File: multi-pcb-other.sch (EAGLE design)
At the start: 6 parts

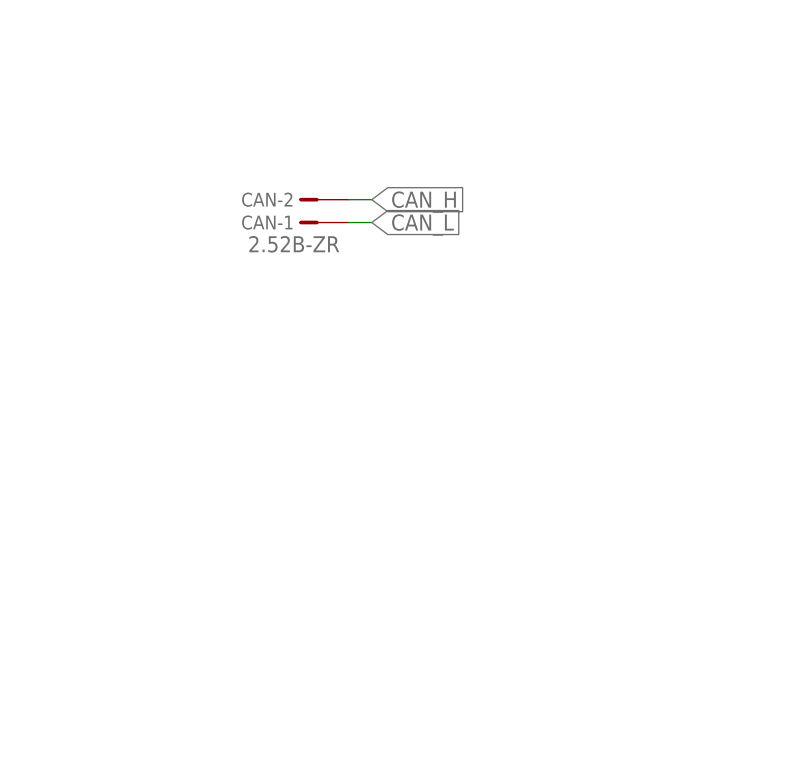
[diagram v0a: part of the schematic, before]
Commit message: Routed more multi-pcb boards
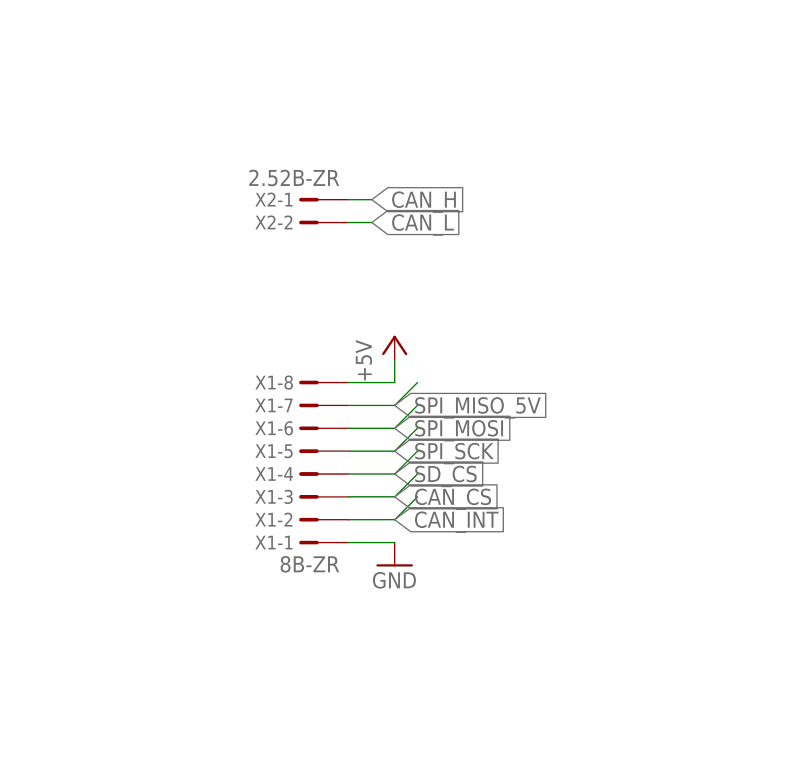
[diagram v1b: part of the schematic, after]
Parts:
- removed CAN: 2.52B-ZR, con-jst-custom:2.52B-ZR
- added X1: 8B-ZR, con-jst-custom:8B-ZR
- added X2: 2.52B-ZR, con-jst-custom:2.52B-ZR
- R14: device rcl:R-EU_0309/10 -> rcl:R-EU_0207/7
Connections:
- net +5V: now also X1-8.1
- net CAN_CS: now also X1-3.1
- net CAN_H: now also X2-1.1; no longer CAN-2.1
- net CAN_INT: now also X1-2.1
- net CAN_L: now also X2-2.1; no longer CAN-1.1
- net GND: now also X1-1.1
- net SD_CS: now also X1-4.1
- net SPI_MISO_5V: now also X1-7.1
- net SPI_MOSI: now also X1-6.1
- net SPI_SCK: now also X1-5.1
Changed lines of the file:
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@@
 <part name="GND7" library="supply1" library_urn="urn:adsk.eagle:library:371" deviceset="GND" device=""/>
 <part name="P+1" library="supply1" library_urn="urn:adsk.eagle:library:371" deviceset="+5V" device=""/>
-<part name="CAN" library="con-jst-custom" deviceset="?2B-ZR" device="2.5" value="2.52B-ZR"/>
 <part name="U$5" library="sd-mmc" deviceset="HKD-MICRO-SD-BREAKOUT" device="H"/>
 <part name="GND24" library="supply1" library_urn="urn:adsk.eagle:library:371" deviceset="GND" device=""/>
 <part name="P+19" library="supply1" library_urn="urn:adsk.eagle:library:371" deviceset="+5V" device=""/>
-<part name="R14" library="rcl" library_urn="urn:adsk.eagle:library:334" deviceset="R-EU_" device="0309/10" package3d_urn="urn:adsk.eagle:package:23567/2" value="2k"/>
+<part name="R14" library="rcl" library_urn="urn:adsk.eagle:library:334" deviceset="R-EU_" device="0207/7" package3d_urn="urn:adsk.eagle:package:23493/2" value="2k"/>
 <part name="R15" library="rcl" library_urn="urn:adsk.eagle:library:334" deviceset="R-EU_" device="0207/7" package3d_urn="urn:adsk.eagle:package:23493/2" value="5k"/>
 <part name="GND30" library="supply1" library_urn="urn:adsk.eagle:library:371" deviceset="GND" device=""/>
 <part name="CAN_TERM_RESISTOR" library="pinhead" library_urn="urn:adsk.eagle:library:325" deviceset="PINHD-1X2" device="" package3d_urn="urn:adsk.eagle:package:22435/2"/>
+<part name="GND1" library="supply1" library_urn="urn:adsk.eagle:library:371" deviceset="GND" device=""/>
+<part name="P+2" library="supply1" library_urn="urn:adsk.eagle:library:371" deviceset="+5V" device=""/>
+<part name="X1" library="con-jst-custom" deviceset="?8B-ZR" device=""/>
+<part name="X2" library="con-jst-custom" deviceset="?2B-ZR" device="2.5"/>
 </parts>
 <sheets>
@@
 <attribute name="VALUE" x="-63.5" y="124.46" size="1.778" layer="96" rot="R180"/>
 </instance>
-<instance part="CAN" gate="-1" x="-167.64" y="96.52" smashed="yes" rot="R180">
-<attribute name="NAME" x="-168.656" y="97.282" size="1.524" layer="95" rot="R180"/>
-<attribute name="VALUE" x="-163.576" y="94.996" size="1.778" layer="96" rot="R180"/>
-</instance>
-<instance part="CAN" gate="-2" x="-167.64" y="99.06" smashed="yes" rot="R180">
-<attribute name="NAME" x="-168.656" y="99.822" size="1.524" layer="95" rot="R180"/>
-</instance>
 <instance part="U$5" gate="G$1" x="50.8" y="78.74" smashed="yes"/>
 <instance part="GND24" gate="1" x="33.02" y="68.58" smashed="yes">
@@
 <attribute name="NAME" x="-176.53" y="-10.795" size="1.778" layer="95" rot="R180"/>
 <attribute name="VALUE" x="-176.53" y="0" size="1.778" layer="96" rot="R180"/>
+</instance>
+<instance part="GND1" gate="1" x="-157.48" y="58.42" smashed="yes">
+<attribute name="VALUE" x="-160.02" y="55.88" size="1.778" layer="96"/>
+</instance>
+<instance part="P+2" gate="1" x="-157.48" y="83.82" smashed="yes">
+<attribute name="VALUE" x="-160.02" y="78.74" size="1.778" layer="96" rot="R90"/>
+</instance>
+<instance part="X1" gate="-1" x="-167.64" y="60.96" smashed="yes" rot="R180">
+<attribute name="NAME" x="-168.656" y="61.722" size="1.524" layer="95" rot="R180"/>
+<attribute name="VALUE" x="-163.576" y="59.436" size="1.778" layer="96" rot="R180"/>
+</instance>
+<instance part="X1" gate="-2" x="-167.64" y="63.5" smashed="yes" rot="R180">
+<attribute name="NAME" x="-168.656" y="64.262" size="1.524" layer="95" rot="R180"/>
+</instance>
+<instance part="X1" gate="-3" x="-167.64" y="66.04" smashed="yes" rot="R180">
+<attribute name="NAME" x="-168.656" y="66.802" size="1.524" layer="95" rot="R180"/>
+</instance>
+<instance part="X1" gate="-4" x="-167.64" y="68.58" smashed="yes" rot="R180">
+<attribute name="NAME" x="-168.656" y="69.342" size="1.524" layer="95" rot="R180"/>
+</instance>
+<instance part="X1" gate="-5" x="-167.64" y="71.12" smashed="yes" rot="R180">
+<attribute name="NAME" x="-168.656" y="71.882" size="1.524" layer="95" rot="R180"/>
+</instance>
+<instance part="X1" gate="-6" x="-167.64" y="73.66" smashed="yes" rot="R180">
+<attribute name="NAME" x="-168.656" y="74.422" size="1.524" layer="95" rot="R180"/>
+</instance>
+<instance part="X1" gate="-7" x="-167.64" y="76.2" smashed="yes" rot="R180">
+<attribute name="NAME" x="-168.656" y="76.962" size="1.524" layer="95" rot="R180"/>
+</instance>
+<instance part="X1" gate="-8" x="-167.64" y="78.74" smashed="yes" rot="R180">
+<attribute name="NAME" x="-168.656" y="79.502" size="1.524" layer="95" rot="R180"/>
+</instance>
+<instance part="X2" gate="-1" x="-167.64" y="99.06" smashed="yes" rot="MR0">
+<attribute name="NAME" x="-168.656" y="98.298" size="1.524" layer="95" rot="MR0"/>
+<attribute name="VALUE" x="-163.576" y="100.584" size="1.778" layer="96" rot="MR0"/>
+</instance>
+<instance part="X2" gate="-2" x="-167.64" y="96.52" smashed="yes" rot="MR0">
+<attribute name="NAME" x="-168.656" y="95.758" size="1.524" layer="95" rot="MR0"/>
 </instance>
 </instances>
@@
 <wire x1="-53.34" y1="157.48" x2="-50.8" y2="157.48" width="0.1524" layer="91"/>
 </segment>
+<segment>
+<pinref part="X1" gate="-1" pin="1"/>
+<pinref part="GND1" gate="1" pin="GND"/>
+<wire x1="-162.56" y1="60.96" x2="-157.48" y2="60.96" width="0.1524" layer="91"/>
+</segment>
 </net>
 <net name="+5V" class="0">
@@
 <wire x1="35.56" y1="73.66" x2="27.94" y2="73.66" width="0.1524" layer="91"/>
 <pinref part="P+19" gate="1" pin="+5V"/>
+</segment>
+<segment>
+<pinref part="P+2" gate="1" pin="+5V"/>
+<wire x1="-157.48" y1="81.28" x2="-157.48" y2="78.74" width="0.1524" layer="91"/>
+<pinref part="X1" gate="-8" pin="1"/>
+<wire x1="-162.56" y1="78.74" x2="-157.48" y2="78.74" width="0.1524" layer="91"/>
 </segment>
 </net>
@@
 <label x="-86.36" y="144.78" size="1.778" layer="95" rot="R90" xref="yes"/>
 </segment>
+<segment>
+<label x="-157.48" y="66.04" size="1.778" layer="95" xref="yes"/>
+<wire x1="-157.48" y1="66.04" x2="-154.94" y2="68.58" width="0.1524" layer="91"/>
+<pinref part="X1" gate="-3" pin="1"/>
+<wire x1="-162.56" y1="66.04" x2="-157.48" y2="66.04" width="0.1524" layer="91"/>
+</segment>
 </net>
 <net name="SPI_MOSI" class="0">
@@
 <label x="33.02" y="78.74" size="1.778" layer="95" rot="R180" xref="yes"/>
 </segment>
+<segment>
+<label x="-157.48" y="73.66" size="1.778" layer="95" xref="yes"/>
+<wire x1="-157.48" y1="73.66" x2="-154.94" y2="76.2" width="0.1524" layer="91"/>
+<pinref part="X1" gate="-6" pin="1"/>
+<wire x1="-162.56" y1="73.66" x2="-157.48" y2="73.66" width="0.1524" layer="91"/>
+</segment>
 </net>
 <net name="SPI_SCK" class="0">
@@
 <wire x1="35.56" y1="81.28" x2="33.02" y2="81.28" width="0.1524" layer="91"/>
 <label x="33.02" y="81.28" size="1.778" layer="95" rot="R180" xref="yes"/>
+</segment>
+<segment>
+<label x="-157.48" y="71.12" size="1.778" layer="95" xref="yes"/>
+<wire x1="-157.48" y1="71.12" x2="-154.94" y2="73.66" width="0.1524" layer="91"/>
+<pinref part="X1" gate="-5" pin="1"/>
+<wire x1="-162.56" y1="71.12" x2="-157.48" y2="71.12" width="0.1524" layer="91"/>
 </segment>
 </net>
@@
 <label x="-66.04" y="160.02" size="1.778" layer="95" rot="R90" xref="yes"/>
 </segment>
+<segment>
+<label x="-157.48" y="63.5" size="1.778" layer="95" xref="yes"/>
+<wire x1="-157.48" y1="63.5" x2="-154.94" y2="66.04" width="0.1524" layer="91"/>
+<pinref part="X1" gate="-2" pin="1"/>
+<wire x1="-162.56" y1="63.5" x2="-157.48" y2="63.5" width="0.1524" layer="91"/>
+</segment>
 </net>
 <net name="CAN_H" class="0">
@@
 </segment>
 <segment>
-<pinref part="CAN" gate="-2" pin="1"/>
 <wire x1="-162.56" y1="99.06" x2="-160.02" y2="99.06" width="0.1524" layer="91"/>
 <label x="-160.02" y="99.06" size="1.778" layer="95" xref="yes"/>
+<pinref part="X2" gate="-1" pin="1"/>
 </segment>
 </net>
@@
 </segment>
 <segment>
-<pinref part="CAN" gate="-1" pin="1"/>
 <wire x1="-162.56" y1="96.52" x2="-160.02" y2="96.52" width="0.1524" layer="91"/>
 <label x="-160.02" y="96.52" size="1.778" layer="95" xref="yes"/>
+<pinref part="X2" gate="-2" pin="1"/>
 </segment>
 </net>
@@
 <wire x1="35.56" y1="83.82" x2="33.02" y2="83.82" width="0.1524" layer="91"/>
 <label x="33.02" y="83.82" size="1.778" layer="95" rot="R180" xref="yes"/>
+</segment>
+<segment>
+<label x="-157.48" y="68.58" size="1.778" layer="95" xref="yes"/>
+<wire x1="-157.48" y1="68.58" x2="-154.94" y2="71.12" width="0.1524" layer="91"/>
+<pinref part="X1" gate="-4" pin="1"/>
+<wire x1="-162.56" y1="68.58" x2="-157.48" y2="68.58" width="0.1524" layer="91"/>
 </segment>
 </net>
@@
 <label x="33.02" y="76.2" size="1.778" layer="95" rot="R180" xref="yes"/>
 </segment>
-</net>
+<segment>
+<label x="-157.48" y="76.2" size="1.778" layer="95" xref="yes"/>
+<wire x1="-157.48" y1="76.2" x2="-154.94" y2="78.74" width="0.1524" layer="91"/>
+<pinref part="X1" gate="-7" pin="1"/>
+<wire x1="-162.56" y1="76.2" x2="-157.48" y2="76.2" width="0.1524" layer="91"/>
+</segment>
+</net>

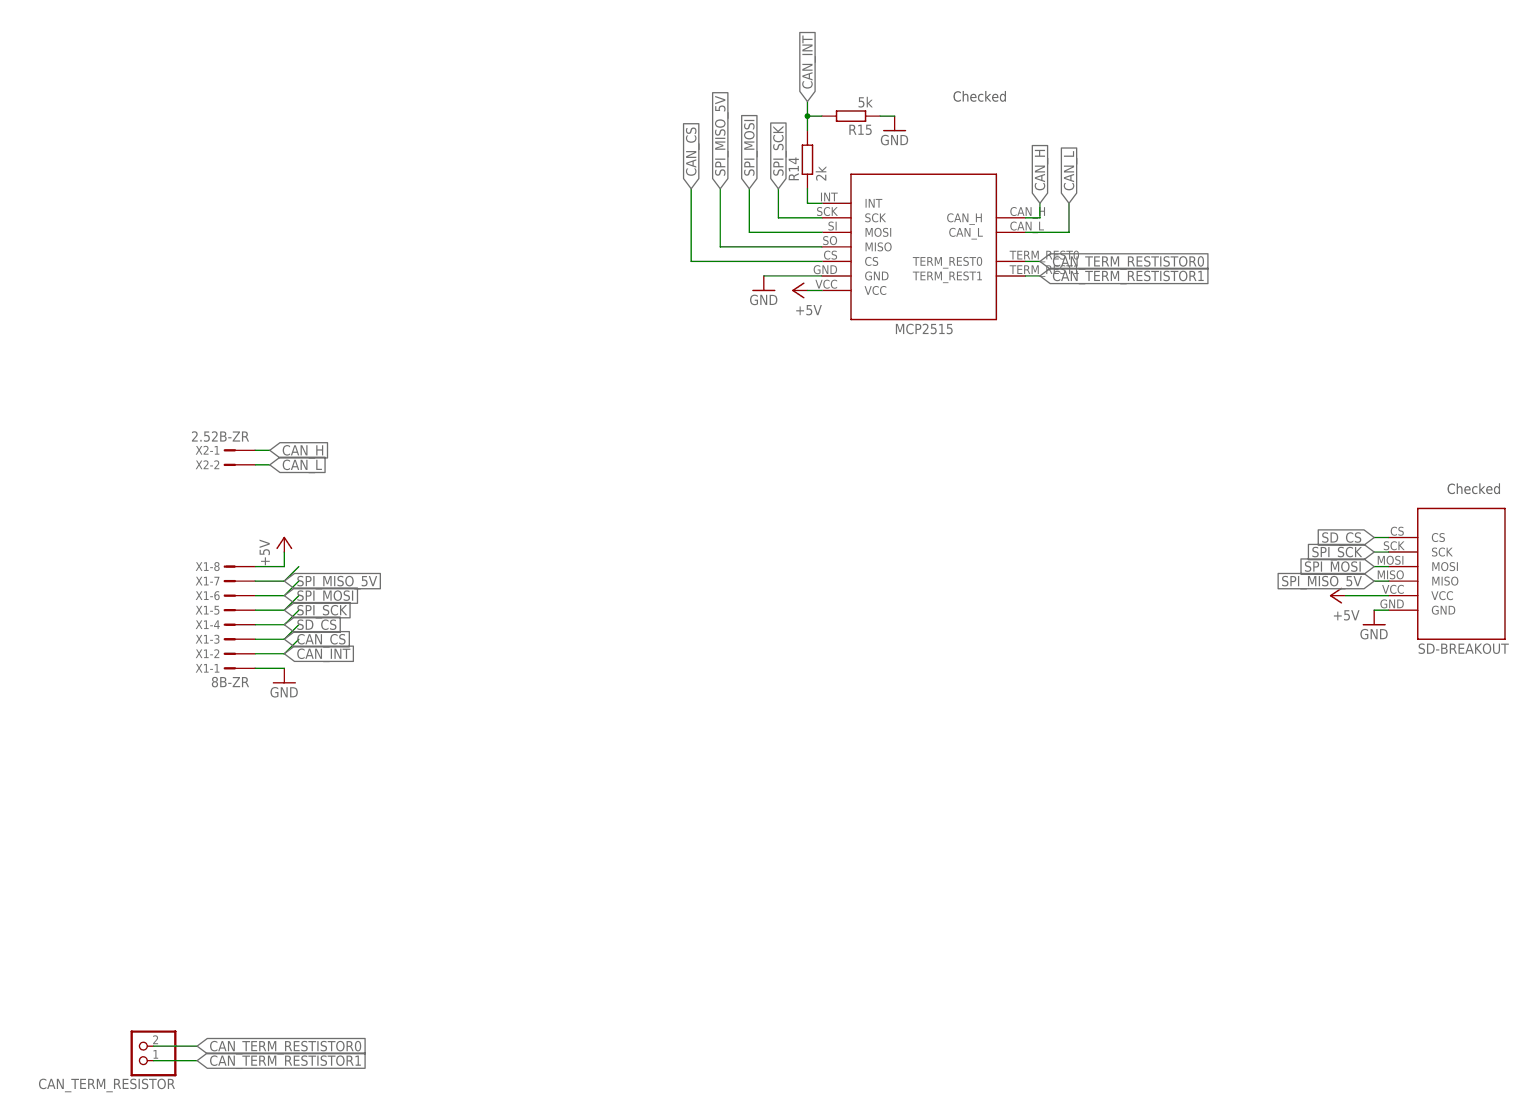
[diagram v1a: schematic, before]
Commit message: Made schematic more compact/clean
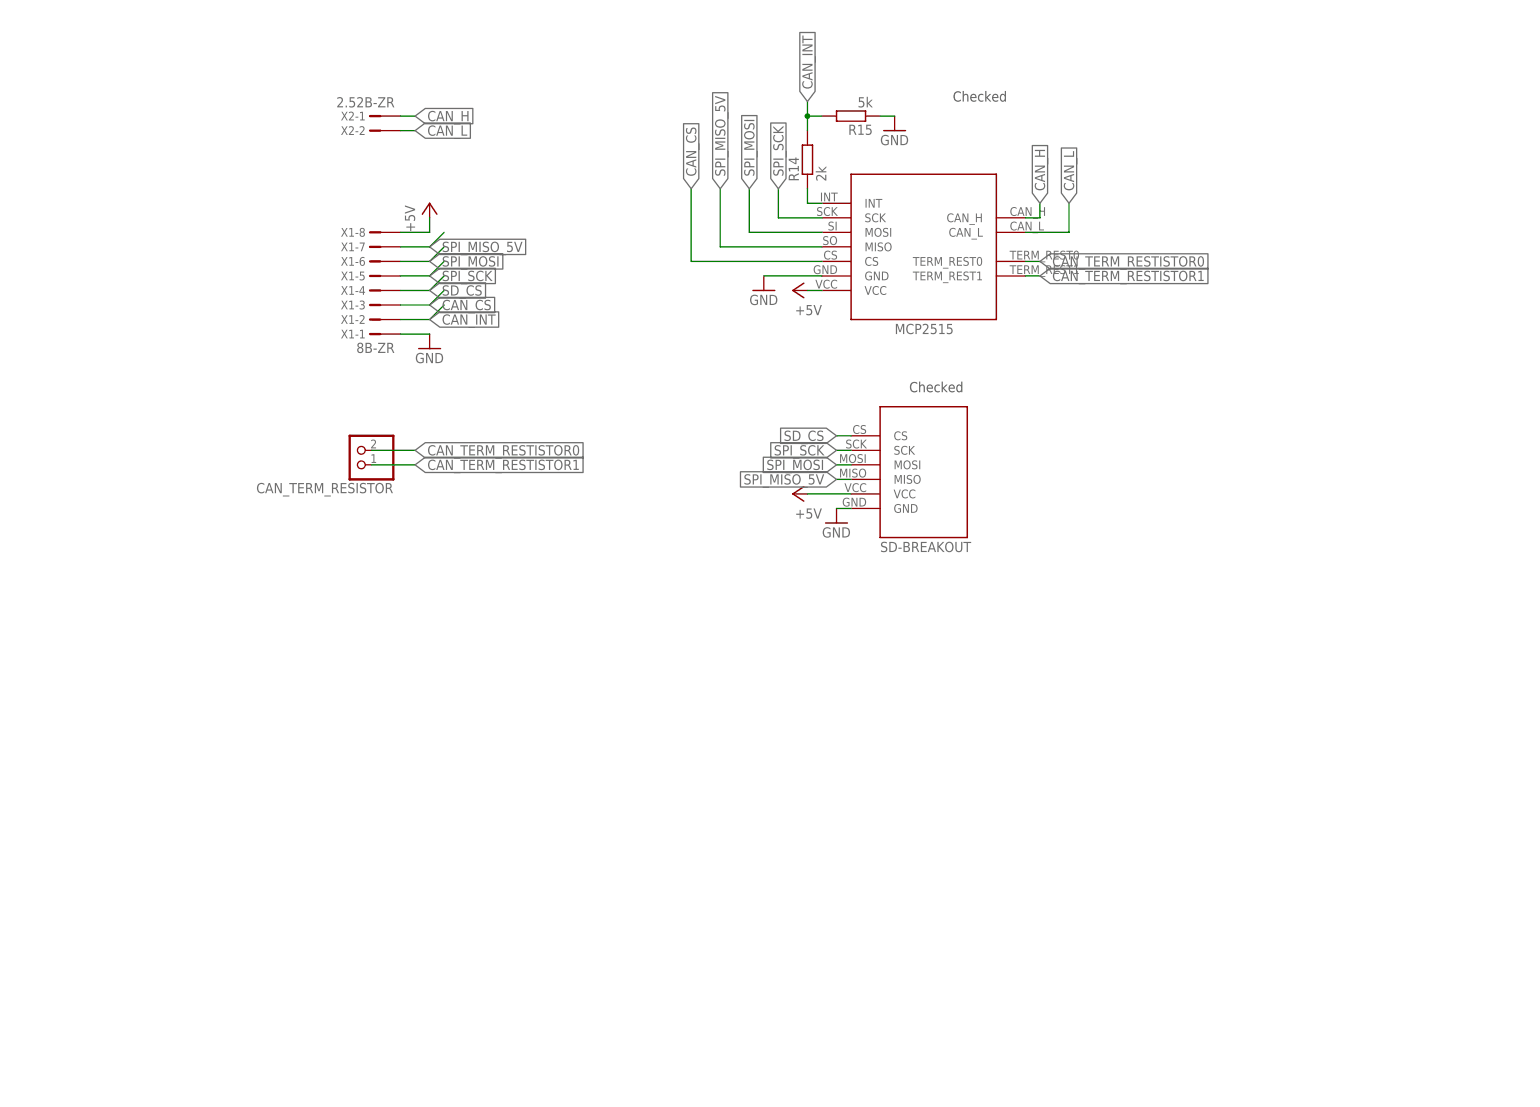
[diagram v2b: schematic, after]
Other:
- moved on the sheet: CAN_TERM_RESISTOR, X1-1, X1-2, X1-3, X1-4, X1-5, X1-6, X1-7, X1-8, X2-1, X2-2

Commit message: Updated trace width and ground plane for others
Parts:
- U$5: device sd-mmc:HKD-MICRO-SD-BREAKOUTH -> samuel:HKD-MICRO-SD-BREAKOUTH
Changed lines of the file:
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@@
 <part name="GND7" library="supply1" library_urn="urn:adsk.eagle:library:371" deviceset="GND" device=""/>
 <part name="P+1" library="supply1" library_urn="urn:adsk.eagle:library:371" deviceset="+5V" device=""/>
-<part name="U$5" library="sd-mmc" deviceset="HKD-MICRO-SD-BREAKOUT" device="H"/>
+<part name="U$5" library="samuel" deviceset="HKD-MICRO-SD-BREAKOUT" device="H"/>
 <part name="GND24" library="supply1" library_urn="urn:adsk.eagle:library:371" deviceset="GND" device=""/>
 <part name="P+19" library="supply1" library_urn="urn:adsk.eagle:library:371" deviceset="+5V" device=""/>

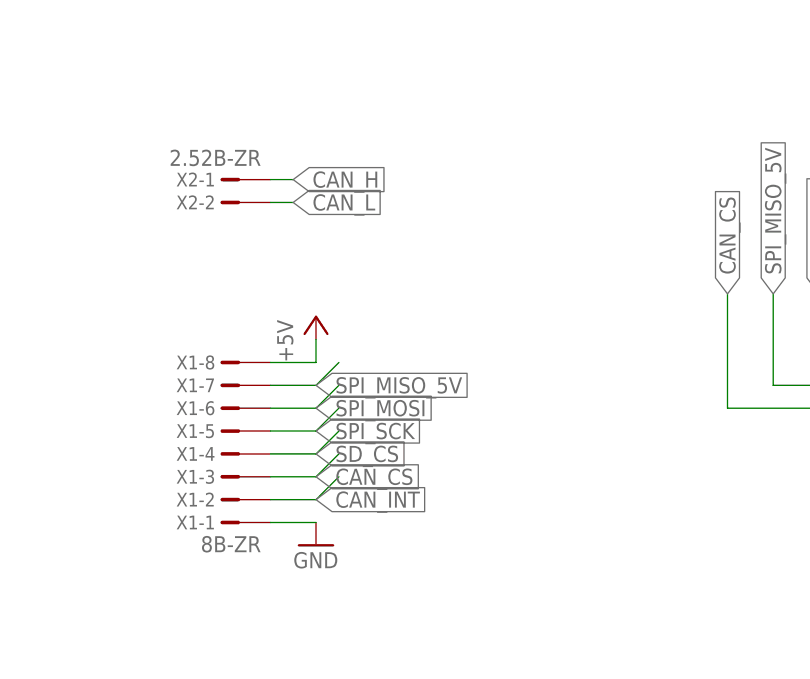
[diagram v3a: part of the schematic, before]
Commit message: PCB layout for multi-pcb-other
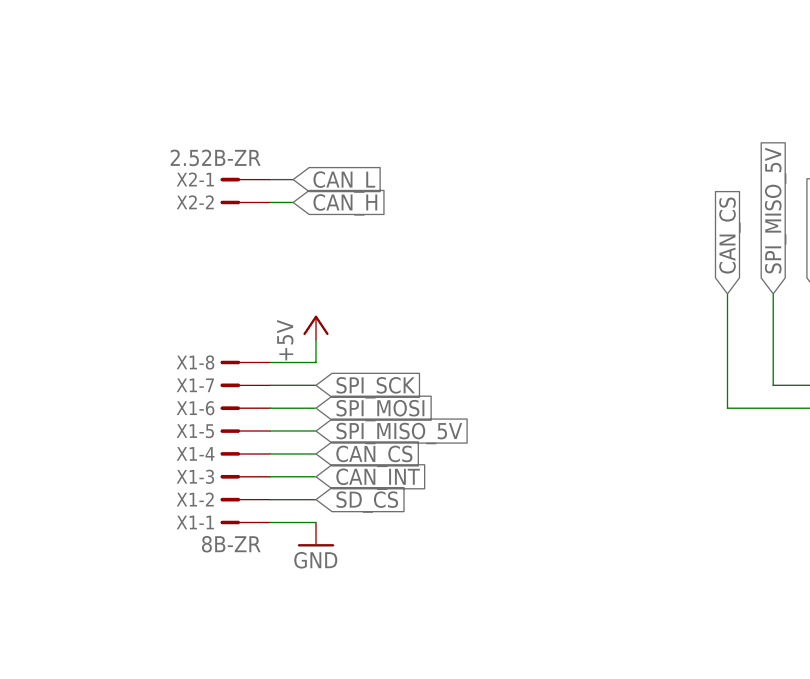
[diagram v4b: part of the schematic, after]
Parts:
- R14, R15: device rcl:R-EU_0207/7 -> rcl:R-EU_0207/10
- U$2: value MCP2515_DEVBOARDINVERTED -> MCP2515_DEVBOARDMCP2515_DEVBOARD_INVERTED_NODRILL; device MCP2515:MCP2515_DEVBOARDINVERTED -> MCP2515:MCP2515_DEVBOARDMCP2515_DEVBOARD_INVERTED_NODRILL
- U$5: value HKD-MICRO-SD-BREAKOUTH -> HKD-MICRO-SD-BREAKOUT; device samuel:HKD-MICRO-SD-BREAKOUTH -> samuel:HKD-MICRO-SD-BREAKOUT
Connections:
- net CAN_CS: now also X1-4.1; no longer X1-3.1
- net CAN_H: now also X2-2.1; no longer X2-1.1
- net CAN_INT: now also X1-3.1; no longer X1-2.1
- net CAN_L: now also X2-1.1; no longer X2-2.1
- net SD_CS: now also X1-2.1; no longer X1-4.1
- net SPI_MISO_5V: now also X1-5.1; no longer X1-7.1
- net SPI_SCK: now also X1-7.1; no longer X1-5.1
